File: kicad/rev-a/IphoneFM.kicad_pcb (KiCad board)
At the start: 2 copper layers, 46.5 x 71.4 mm, 106 parts, among them J1 USB 2.0 Type-C, J2 SMA jack, SW1 SPDT, SW2 SPST, SW3 6 × SPST, U1 MCU, U2 Synthesizer, U3 3.3 V 600 mA LDO, U4 FM receiver, U5 SPDT RF switch, U6 USB ESD array, U7 Digital step attenuator, Y2 20 MHz CMOS XO

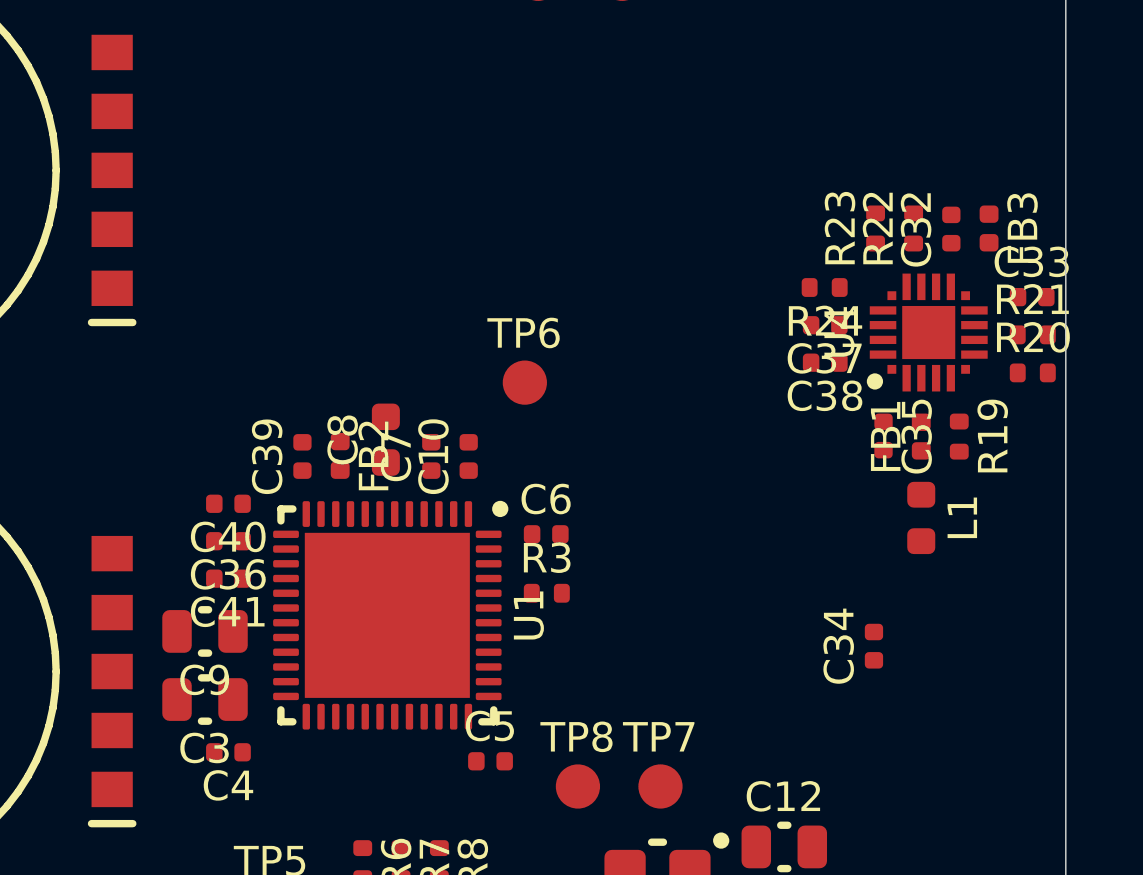
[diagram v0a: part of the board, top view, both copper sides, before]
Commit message: U1 pins reassigned for the turned U1 of floorplan B3: receiver lines (PB6 FS, PB8 SCL, PB9 RCLK, PB4 RST) and U2 CE (PH1) on the U4/U2 sides, LEDs on PA0-PA2 (TIM2), wheels on PA3-PA5, RF_MODE PA7, CC on PB0/PB1; each checked against DS14217 Tables 26-28 and p132 and AN2606 Table 165; C36/C39/C40 follow their nets; U4 group 0.6 mm in from the edge
Co-Authored-By: Claude Opus 5.5 <noreply@anthropic.com>
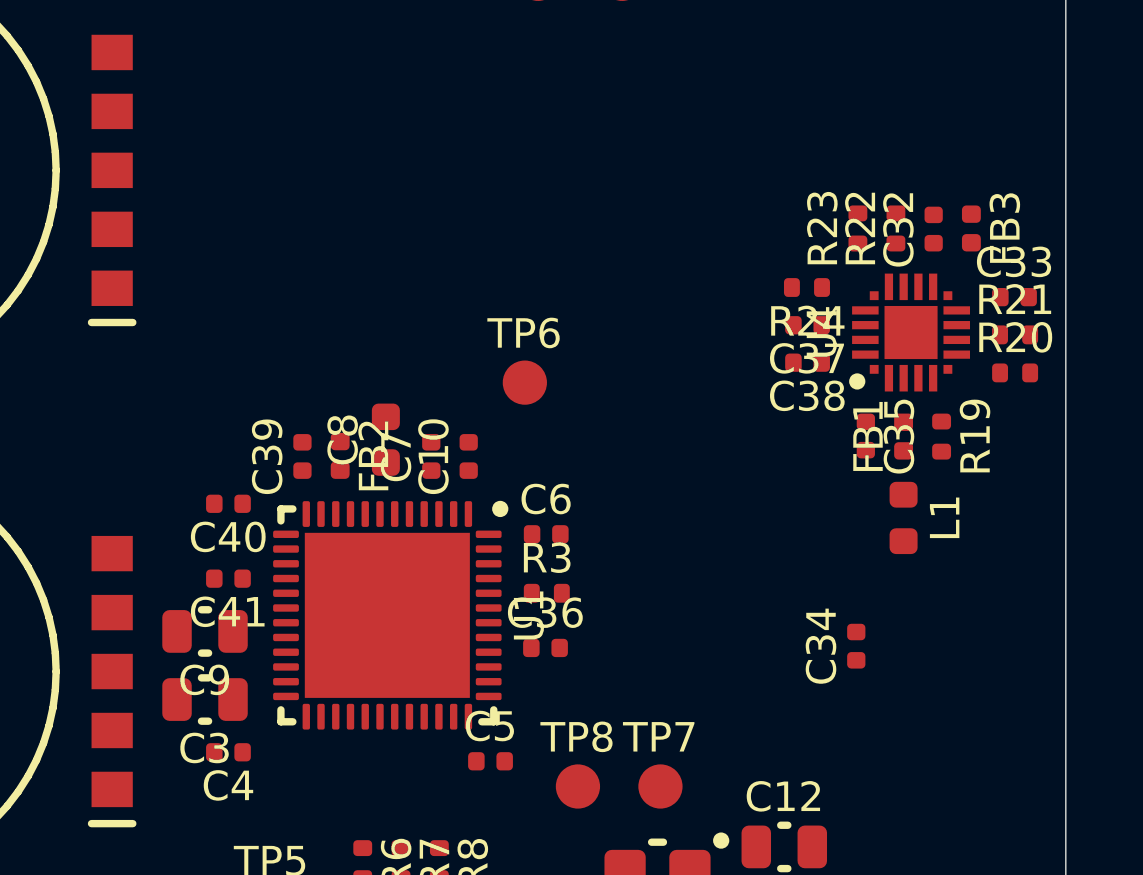
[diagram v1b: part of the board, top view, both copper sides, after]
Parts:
- moved C36 11.3 mm to (41.5, 94.2), turned to 0 degrees
- moved C32 0.60 mm to (54.7, 80.0)
- moved C33 0.60 mm to (57.4, 82.3)
- moved C34 0.60 mm to (52.0, 94.1)
- moved C35 0.60 mm to (52.4, 87.0)
- moved C37 0.60 mm to (50.4, 83.3)
- moved C38 0.60 mm to (50.4, 84.5)
- moved FB1 0.60 mm to (53.6, 87.0)
- moved FB3 0.60 mm to (55.9, 80.0)
- moved L1 0.60 mm to (53.6, 89.8)
- moved R19 0.60 mm to (54.9, 87.0)
- moved R20 0.60 mm to (57.4, 84.9)
- moved R21 0.60 mm to (57.4, 83.6)
- moved R23 0.60 mm to (52.1, 80.0)
- moved R24 0.60 mm to (50.4, 82.0)
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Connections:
- U1 pad 10: /CC1 -> /LED_R
- U1 pad 11: /CC2 -> /LED_G
- U1 pad 12: /WHEEL1 -> /LED_B
- U1 pad 13: /WHEEL2 -> /WHEEL1
- U1 pad 14: /RX_FS_MCU -> /WHEEL2
- U1 pad 16: /RX_RST -> unconnected-(U1-PA6-Pad16)
- U1 pad 17: unconnected-(U1-PA7-Pad17) -> /RF_MODE
- U1 pad 18: /RF_MODE -> /CC1
- U1 pad 19: /LED_B -> /CC2
- U1 pad 20: /LMX_CE -> unconnected-(U1-PB2-Pad20)
- U1 pad 21: /LED_G -> unconnected-(U1-PB10-Pad21)
- U1 pad 40: /LED_R -> /RX_RST
- U1 pad 42: /I2C_SCL -> /RX_FS_MCU
- U1 pad 45: /RX_RCLK -> /I2C_SCL
- U1 pad 46: unconnected-(U1-PB9-Pad46) -> /RX_RCLK
- U1 pad 6: unconnected-(U1-PH1-Pad6) -> /LMX_CE

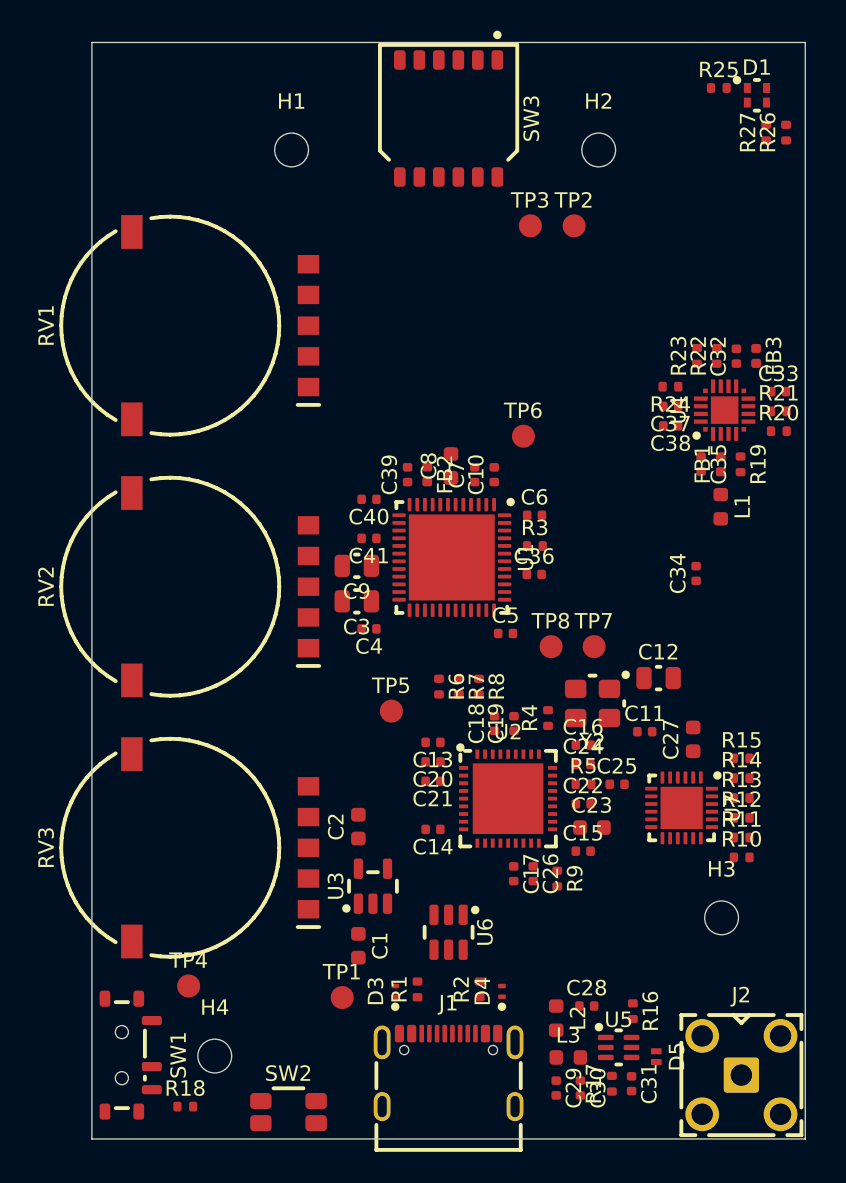
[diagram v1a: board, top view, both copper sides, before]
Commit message: Phase 5 prep for B3: RF keep-out zones, RF lines planned (pcb_route_rf.py place/lay) with 12 part nudges, routing-quality checker (pcb_quality.py), lane plan for review
Co-Authored-By: Claude Opus 5.5 <noreply@anthropic.com>
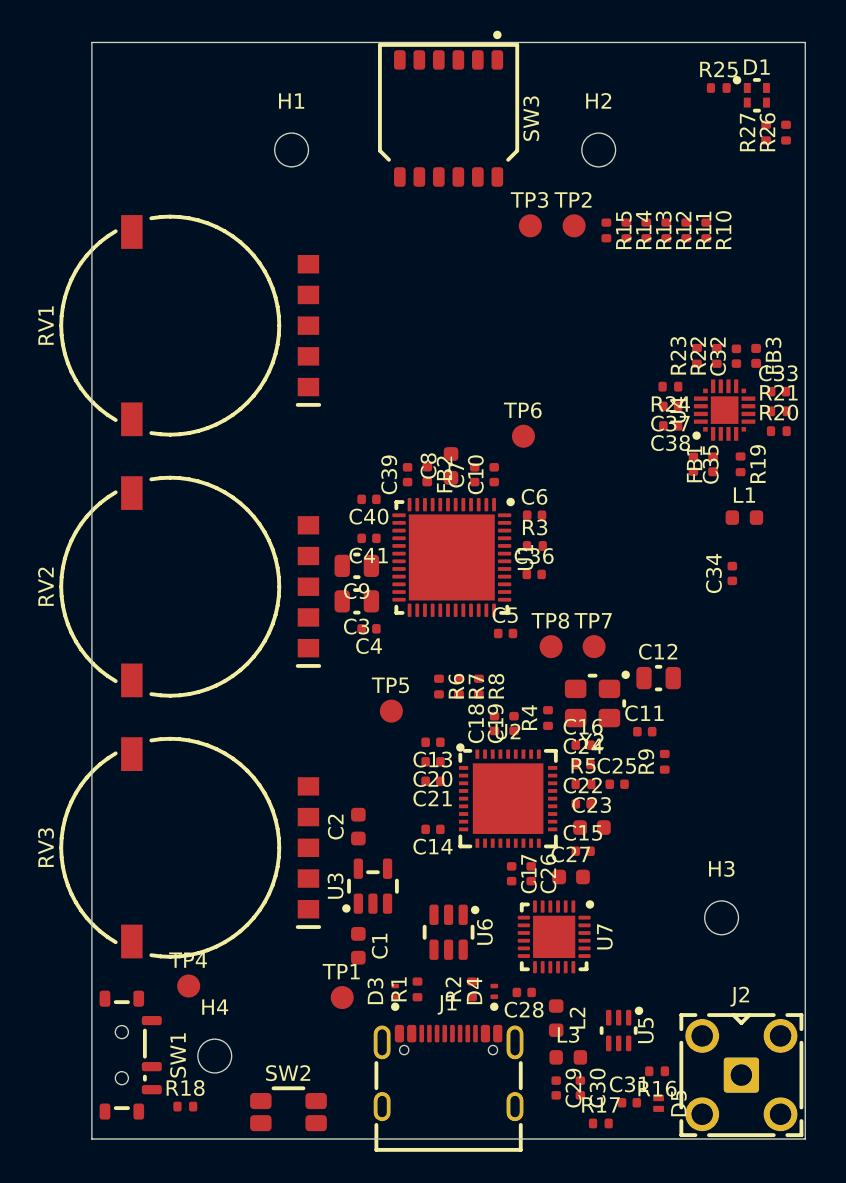
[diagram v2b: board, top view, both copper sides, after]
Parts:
- moved R10 40.9 mm to (52.7, 71.8), turned to -90 degrees
- moved R11 39.7 mm to (51.4, 71.8), turned to -90 degrees
- moved R12 38.6 mm to (50.1, 71.8), turned to -90 degrees
- moved R13 37.5 mm to (48.8, 71.8), turned to -90 degrees
- moved R14 36.4 mm to (47.5, 71.8), turned to -90 degrees
- moved R15 35.5 mm to (46.2, 71.8), turned to -90 degrees
- moved C27 12.0 mm to (43.9, 113.9), turned to 0 degrees
- moved U7 11.8 mm to (42.8, 117.8)
- moved R9 10.3 mm to (50.0, 106.4), turned to 90 degrees
- moved R16 4.22 mm to (49.5, 126.5), turned to 180 degrees
- moved C28 4.17 mm to (40.9, 121.4), turned to 180 degrees
- moved D5 3.05 mm to (49.6, 128.7)
- moved R17 2.69 mm to (45.8, 129.9), turned to 0 degrees
- moved C34 2.36 mm to (54.4, 94.1)
- moved L1 1.70 mm to (55.2, 90.5), turned to 0 degrees
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
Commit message: Phase 5 prep: RX_RST to PB9 and RX_RCLK to PB4 (TIM3_CH1), U4 corner planned (pcb_route_u4.py) with U4's group 2.5 mm lower, U2 east caps re-stacked for CE, Y2/R4/C11/C12/R9/C5/C18/C19/TP7 and U3 group re-seated, C36 to R23 and R3 to SW2, lane plan rev 2
Co-Authored-By: Claude Opus 5.5 <noreply@anthropic.com>
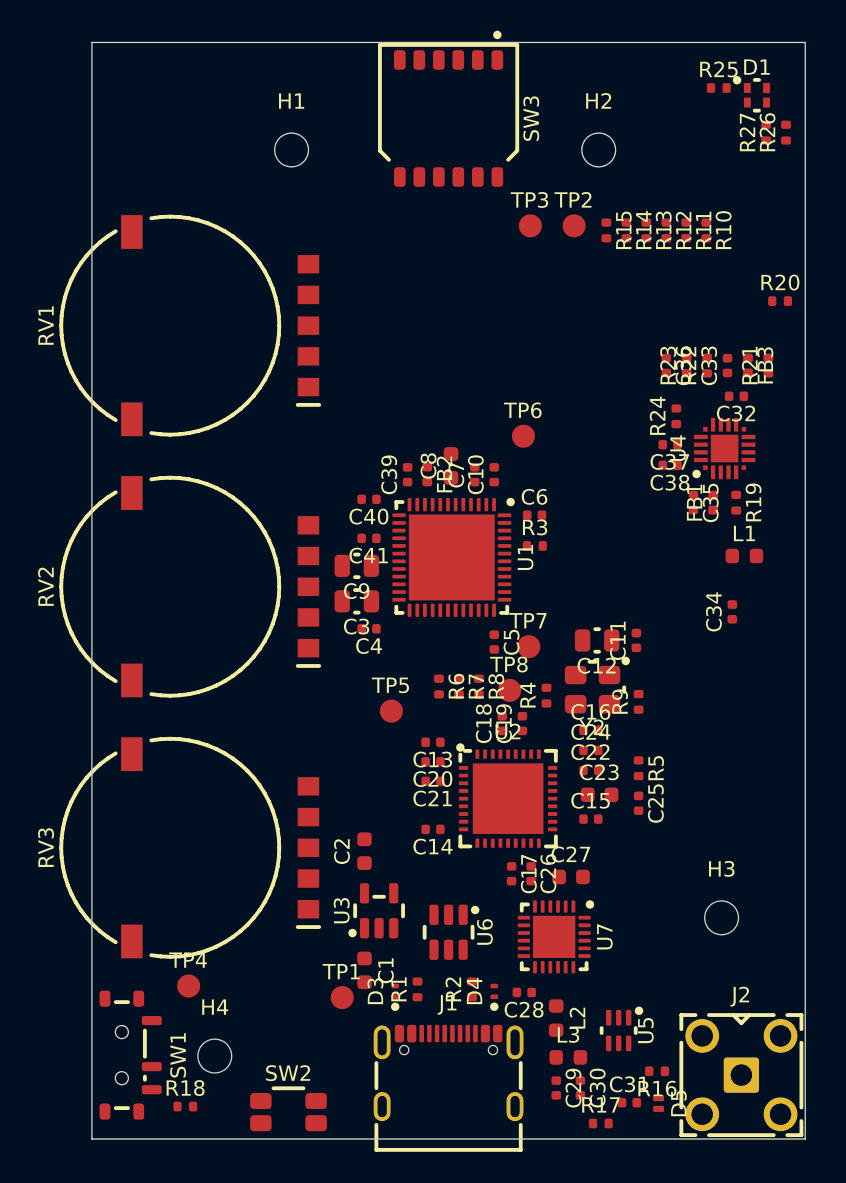
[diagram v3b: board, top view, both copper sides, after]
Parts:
- moved C36 16.1 mm to (50.1, 80.6), turned to -90 degrees
- moved R20 8.47 mm to (57.5, 76.4)
- moved C11 5.97 mm to (48.1, 98.5), turned to 90 degrees
- moved C12 4.69 mm to (45.6, 98.5), turned to 180 degrees
- moved R9 4.25 mm to (48.3, 102.5)
- moved TP7 4.25 mm to (41.1, 98.9)
- moved TP8 3.93 mm to (39.9, 101.8)
- moved R5 3.74 mm to (48.3, 106.8), turned to -90 degrees
- moved C33 3.73 mm to (54.1, 80.6), turned to 90 degrees
- moved R21 3.06 mm to (56.8, 80.6), turned to 90 degrees
- moved C32 2.61 mm to (54.7, 82.6), turned to 180 degrees
- moved C38 2.58 mm to (50.4, 87.1)
- moved R19 2.52 mm to (54.6, 89.5)
- moved C34 2.50 mm to (54.4, 96.6)
- moved C35 2.50 mm to (51.9, 89.5)
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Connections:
- U1 pad 40: /RX_RST -> /RX_RCLK
- U1 pad 46: /RX_RCLK -> /RX_RST

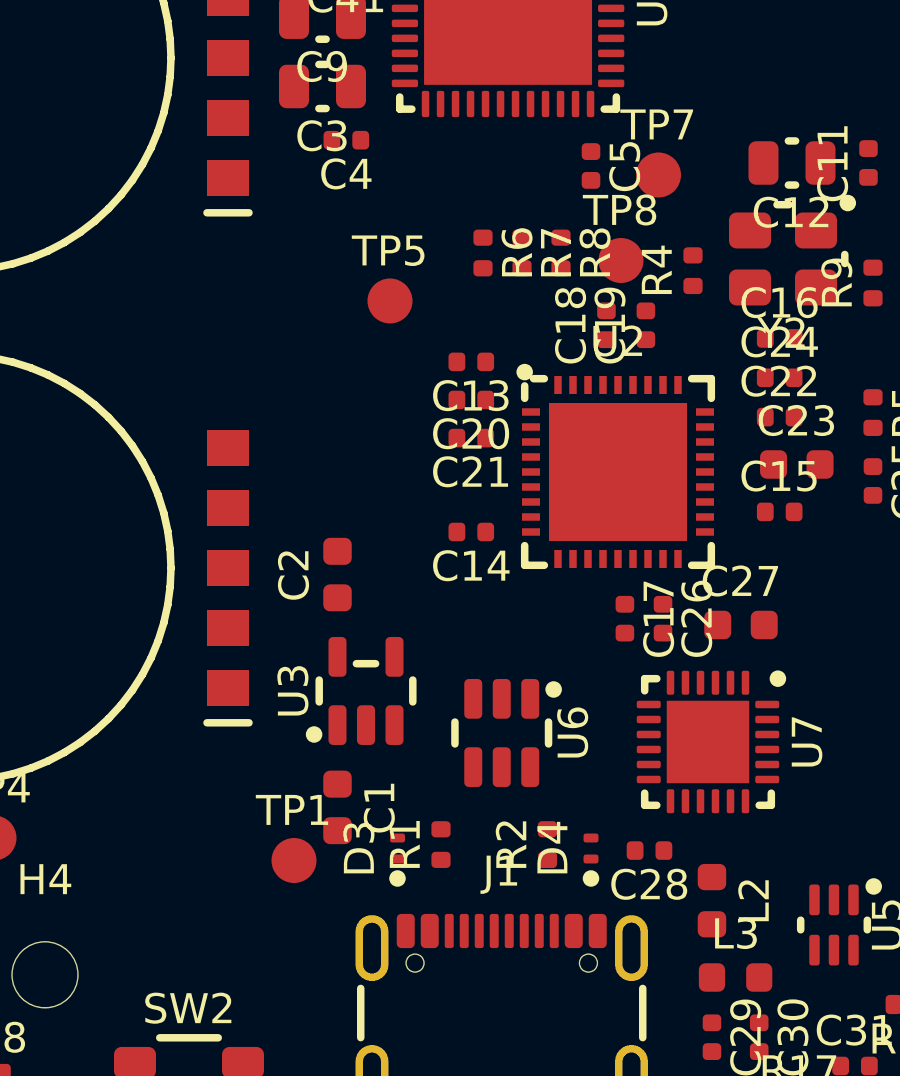
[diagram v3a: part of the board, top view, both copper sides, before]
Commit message: Phase 5 prep: TP1, TP5 and TP8 on the bottom side as bare pads; test pads out of the position files
Co-Authored-By: Claude Opus 5.5 <noreply@anthropic.com>
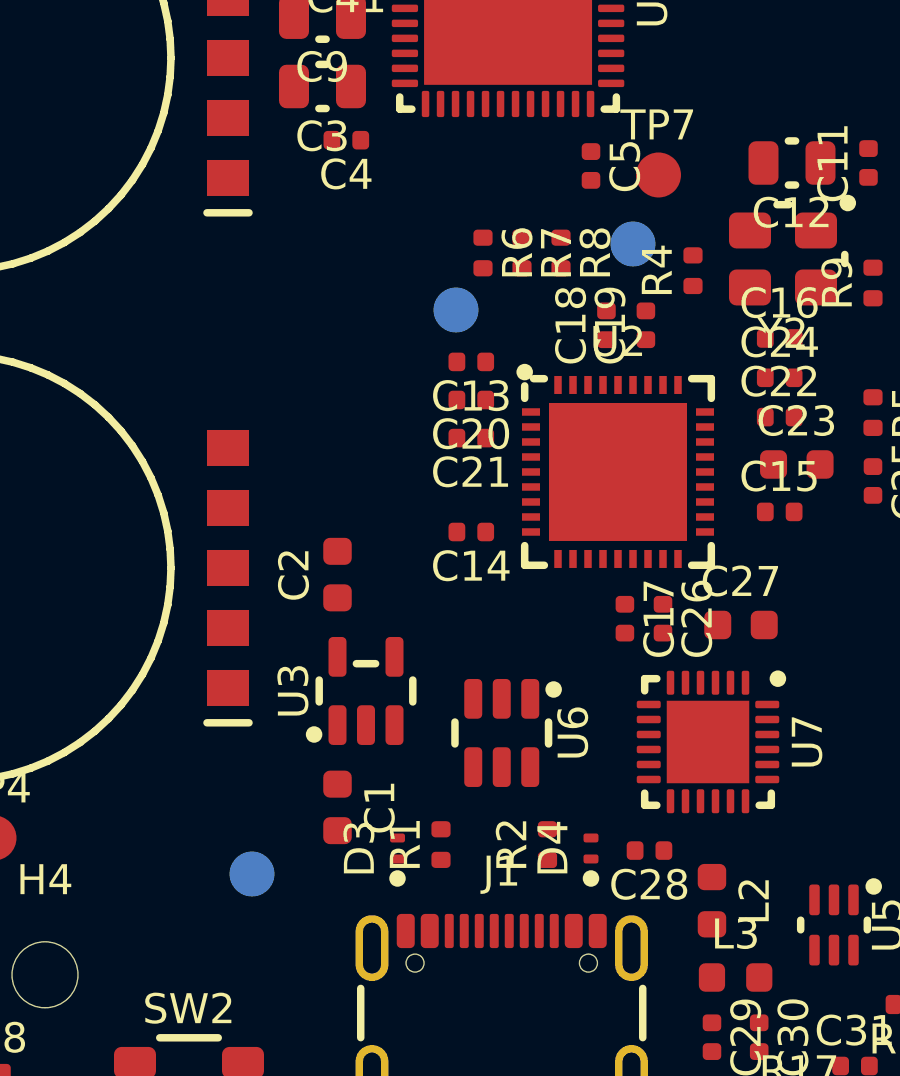
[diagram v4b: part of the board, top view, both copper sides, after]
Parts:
- TP1, TP5, TP8: moved to B.Cu
- moved TP5 2.22 mm to (34.4, 103.4), turned to 180 degrees
- moved TP1 1.47 mm to (27.6, 122.2), turned to 180 degrees
- moved TP8 0.68 mm to (40.3, 101.2), turned to 180 degrees
